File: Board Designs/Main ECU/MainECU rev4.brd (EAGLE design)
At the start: 120.6 x 78.9 mm, 164 parts, among them Q10 MMBT3904LT3G, Q11 MMBT3904LT3G, Q9 MMBT3904LT3G, X1 CONNECTOR-37, X2 CONNECTOR-4AUTOSPORT, X3 CONNECTOR-4NANO-FIT-VERTICAL-4, X4 CONNECTOR-4NANO-FIT-VERTICAL-4

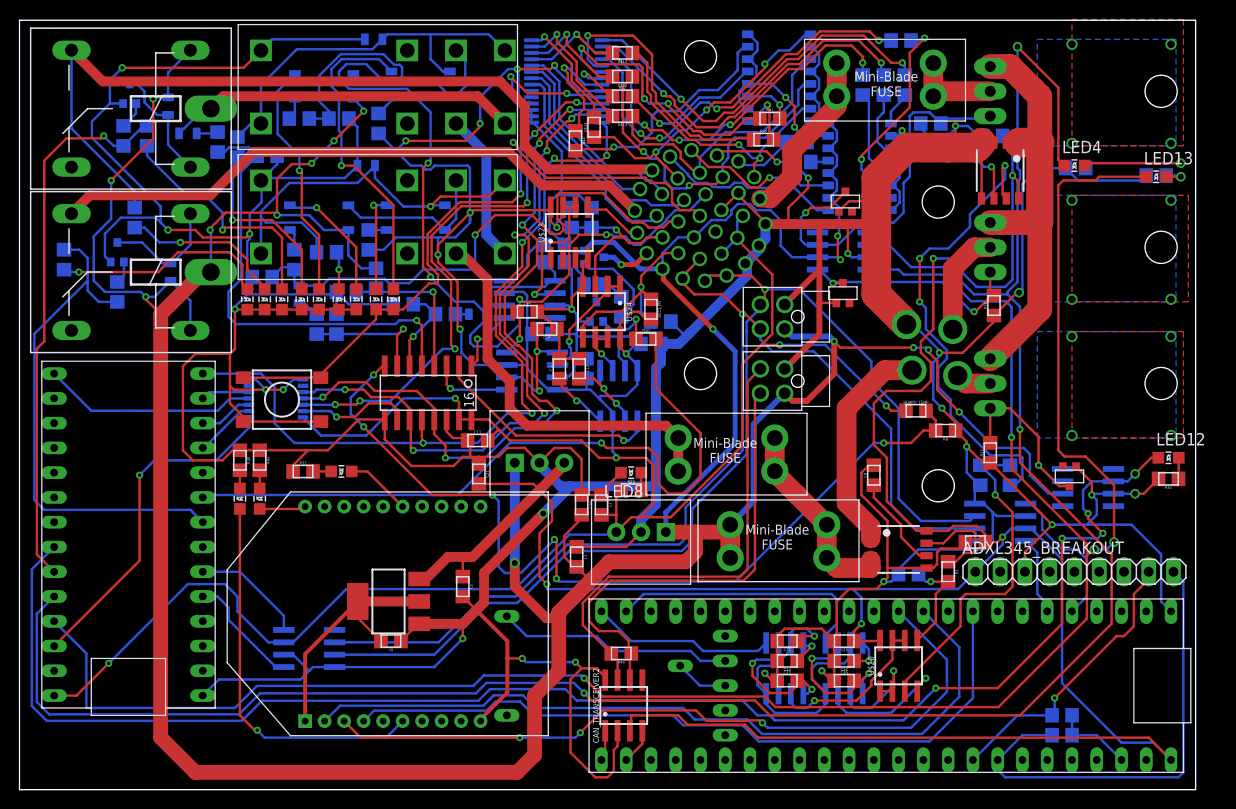
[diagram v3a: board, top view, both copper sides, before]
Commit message: Main ECU rev4: Flip transistors to top layer, widen inverter supply trace, move some resistors for easier soldering, adjust dashboard control resistor values, clean up schematic
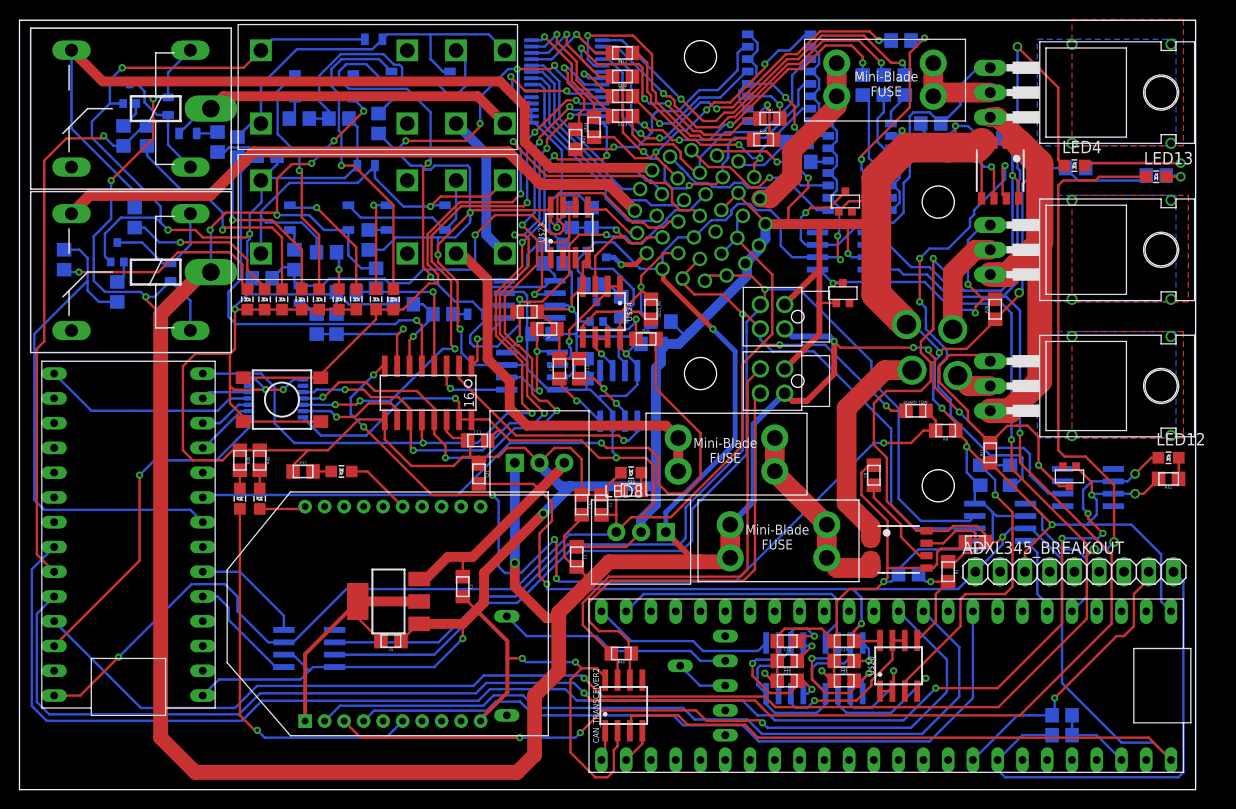
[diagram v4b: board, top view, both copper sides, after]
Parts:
- R35, R36, R38, R39, R40, R41, R42: value 2.2k -> 150
- R43: value 0 -> 150
- R44: value 2.2k -> 0
- moved R43 22.7 mm to (57.0, 66.7), flipped to the top, turned to 270 degrees
- moved R44 22.7 mm to (79.8, 66.4), flipped to the bottom, turned to 0 degrees
- moved R28 0.40 mm to (100.1, 49.3)
- moved R7 0.25 mm to (43.4, 48.8)
- moved U$15 0.25 mm to (59.2, 54.6)
- moved U$4 0.25 mm to (105.9, 55.4), flipped to the top, turned to 270 degrees
- moved U$6 0.25 mm to (105.9, 41.4), flipped to the top, turned to 270 degrees
- moved C10 0.25 mm to (99.8, 66.8)
- moved C19 0.18 mm to (54.7, 54.0)
- moved D2 0.13 mm to (46.9, 48.8)
- moved R18 0.13 mm to (24.9, 52.5)
- moved C17 0.13 mm to (54.7, 55.9)
- moved U$7 0.13 mm to (105.9, 71.5), flipped to the top, turned to 270 degrees
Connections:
- net DASH_CTRL8_OUT: now also R43.1; no longer R44.1
- net DASH_IO1: now also R44.2; no longer R43.2
- net N$57: now also R43.2; no longer R44.2
- net N$59: now also R44.1; no longer R43.1
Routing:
- net PUMPDRIVE: track 19.9 -> 32.3 mm
- net FAN2DRIVE: track 24.3 -> 31.8 mm, vias 2 -> 3
- net FAN2CONTROL: track 223.7 -> 220.1 mm
- net FAN1DRIVE: track 39.4 -> 42.7 mm
- net +12V: track 419.0 -> 417.5 mm
- net GND: track 845.5 -> 844.9 mm

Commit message: Main ECU rev{2,4}: Specify PNP transistor P/Ns
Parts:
- U$15: value BJT_PNPSOT -> SMMBT2907ALT1G
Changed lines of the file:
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@@
 </element>
 <element name="Q10" library="HyTechDevices" package="SOT23" value="MMBT3904LT3G" x="59.182" y="49.022" smashed="yes" rot="MR0"/>
-<element name="U$15" library="HyTechDevices" package="SOT23" value="BJT_PNPSOT" x="59.182" y="54.61" smashed="yes" rot="MR90"/>
+<element name="U$15" library="HyTechDevices" package="SOT23" value="SMMBT2907ALT1G" x="59.182" y="54.61" smashed="yes" rot="MR90"/>
 <element name="R10" library="HyTechDevices" package="0805" value="2.2k" x="64.262" y="46.228" smashed="yes">
 <attribute name="NAME" x="64.262" y="46.9519" size="0.3048" layer="25" align="bottom-center"/>

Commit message: Main ECU rev{1-4}: Add warning about RTC cell assembly, specify current sensor input capacitor value, lower XBee LED resistor to 33R; Main ECU rev{2,4}: Specify MCP3208 input capacitor value; Main ECU rev4: Lower relay-controlling transistors' base resistor to 1k; Main ECU rev5: make all relevant changes previously listed
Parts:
- C10, C9: value (none) -> 0.1uF
- C11: value (none) -> 1uF
- R45: value 2.3k -> 33
- R47, R50: value 2.2k -> 1k
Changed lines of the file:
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@@
 <attribute name="VALUE" x="56.4388" y="23.876" size="0.3048" layer="27" rot="R270" align="top-center"/>
 </element>
-<element name="C10" library="HyTechDevices" package="0805" value="" x="99.822" y="66.802" smashed="yes" rot="MR0">
+<element name="C10" library="HyTechDevices" package="0805" value="0.1uF" x="99.822" y="66.802" smashed="yes" rot="MR0">
 <attribute name="NAME" x="99.822" y="67.5259" size="0.3048" layer="26" rot="MR0" align="bottom-center" display="off"/>
 <attribute name="VALUE" x="99.822" y="66.0908" size="0.3048" layer="28" rot="MR0" align="top-center"/>
@@
 <attribute name="VALUE" x="88.3412" y="32.258" size="0.3048" layer="27" rot="R90" align="top-center"/>
 </element>
-<element name="C9" library="HyTechDevices" package="0805" value="" x="98.044" y="25.4" smashed="yes" rot="R180">
+<element name="C9" library="HyTechDevices" package="0805" value="0.1uF" x="98.044" y="25.4" smashed="yes" rot="R180">
 <attribute name="NAME" x="98.044" y="24.6761" size="0.3048" layer="25" rot="R180" align="bottom-center"/>
 <attribute name="VALUE" x="98.044" y="26.1112" size="0.3048" layer="27" rot="R180" align="top-center"/>
@@
 <attribute name="VALUE" x="79.756" y="65.7098" size="0.3048" layer="28" rot="MR0" align="top-center"/>
 </element>
-<element name="R45" library="HyTechDevices" package="0805" value="2.3k" x="24.638" y="33.782" smashed="yes" rot="R270">
+<element name="R45" library="HyTechDevices" package="0805" value="33" x="24.638" y="33.782" smashed="yes" rot="R270">
 <attribute name="NAME" x="25.3619" y="33.782" size="0.3048" layer="25" rot="R270" align="bottom-center"/>
 <attribute name="VALUE" x="23.9268" y="33.782" size="0.3048" layer="27" rot="R270" align="top-center"/>
@@
 <attribute name="VALUE" x="46.4058" y="32.385" size="0.3048" layer="27" rot="R270" align="top-center"/>
 </element>
-<element name="C11" library="HyTechDevices" package="0805" value="" x="46.99" y="35.814" smashed="yes">
+<element name="C11" library="HyTechDevices" package="0805" value="1uF" x="46.99" y="35.814" smashed="yes">
 <attribute name="NAME" x="46.99" y="36.5379" size="0.3048" layer="25" align="bottom-center"/>
 <attribute name="VALUE" x="46.99" y="35.1028" size="0.3048" layer="27" align="top-center"/>
@@
 </element>
 <element name="Q9" library="HyTechDevices" package="SOT23" value="MMBT3904LT3G" x="10.033" y="55.118" smashed="yes" rot="MR0"/>
-<element name="R47" library="HyTechDevices" package="0805" value="2.2k" x="10.033" y="51.054" smashed="yes" rot="MR90">
+<element name="R47" library="HyTechDevices" package="0805" value="1k" x="10.033" y="51.054" smashed="yes" rot="MR90">
 <attribute name="NAME" x="10.7569" y="51.054" size="0.3048" layer="26" rot="MR90" align="bottom-center"/>
 <attribute name="VALUE" x="9.3218" y="51.054" size="0.3048" layer="28" rot="MR90" align="top-center"/>
 </element>
 <element name="Q11" library="HyTechDevices" package="SOT23" value="MMBT3904LT3G" x="11.303" y="71.374" smashed="yes" rot="MR0"/>
-<element name="R50" library="HyTechDevices" package="0805" value="2.2k" x="10.668" y="67.056" smashed="yes" rot="MR90">
+<element name="R50" library="HyTechDevices" package="0805" value="1k" x="10.668" y="67.056" smashed="yes" rot="MR90">
 <attribute name="NAME" x="11.3919" y="67.056" size="0.3048" layer="26" rot="MR90" align="bottom-center"/>
 <attribute name="VALUE" x="9.9568" y="67.056" size="0.3048" layer="28" rot="MR90" align="top-center"/>

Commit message: Main ECU rev{1-5}: Update values of LED resistors based on testing
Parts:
- R11: value 43 -> 150
- R14, R21: value 820 -> 2k
- R16, R25, R32, R51, R52: value 100 -> 1.2k
- R17: value 820 -> 20k
- R31: value 1.2K -> 6.8k
- R45: value 33 -> 0
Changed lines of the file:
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@@
 <attribute name="VALUE" x="94.5388" y="22.352" size="0.3048" layer="27" rot="R270" align="top-center"/>
 </element>
-<element name="R11" library="HyTechDevices" package="0805" value="43" x="28.702" y="68.834" smashed="yes" rot="MR180">
+<element name="R11" library="HyTechDevices" package="0805" value="150" x="28.702" y="68.834" smashed="yes" rot="MR180">
 <attribute name="NAME" x="28.702" y="68.1101" size="0.3048" layer="26" rot="MR180" align="bottom-center"/>
 <attribute name="VALUE" x="28.702" y="69.5452" size="0.3048" layer="28" rot="MR180" align="top-center"/>
@@
 <attribute name="VALUE" x="36.1188" y="68.326" size="0.3048" layer="28" rot="MR90" align="top-center"/>
 </element>
-<element name="R14" library="HyTechDevices" package="0805" value="820" x="31.496" y="55.118" smashed="yes" rot="MR180">
+<element name="R14" library="HyTechDevices" package="0805" value="2k" x="31.496" y="55.118" smashed="yes" rot="MR180">
 <attribute name="NAME" x="31.496" y="54.3941" size="0.3048" layer="26" rot="MR180" align="bottom-center"/>
 <attribute name="VALUE" x="31.496" y="55.8292" size="0.3048" layer="28" rot="MR180" align="top-center"/>
@@
 <attribute name="VALUE" x="21.0312" y="66.421" size="0.3048" layer="28" rot="MR270" align="top-center"/>
 </element>
-<element name="R17" library="HyTechDevices" package="0805" value="820" x="22.352" y="65.913" smashed="yes" rot="MR270">
+<element name="R17" library="HyTechDevices" package="0805" value="20k" x="22.352" y="65.913" smashed="yes" rot="MR270">
 <attribute name="NAME" x="21.6281" y="65.913" size="0.3048" layer="26" rot="MR270" align="bottom-center"/>
 <attribute name="VALUE" x="23.0632" y="65.913" size="0.3048" layer="28" rot="MR270" align="top-center"/>
@@
 <attribute name="VALUE" x="62.738" y="30.0228" size="0.3048" layer="27" align="top-center"/>
 </element>
-<element name="R21" library="HyTechDevices" package="0805" value="820" x="28.194" y="54.356" smashed="yes" rot="MR90">
+<element name="R21" library="HyTechDevices" package="0805" value="2k" x="28.194" y="54.356" smashed="yes" rot="MR90">
 <attribute name="NAME" x="28.9179" y="54.356" size="0.3048" layer="26" rot="MR90" align="bottom-center"/>
 <attribute name="VALUE" x="27.4828" y="54.356" size="0.3048" layer="28" rot="MR90" align="top-center"/>
@@
 <attribute name="VALUE" x="21.8948" y="33.782" size="0.3048" layer="27" rot="R270" align="top-center"/>
 </element>
-<element name="R31" library="HyTechDevices" package="0805" value="1.2K" x="11.811" y="58.674" smashed="yes" rot="MR270">
+<element name="R31" library="HyTechDevices" package="0805" value="6.8k" x="11.811" y="58.674" smashed="yes" rot="MR270">
 <attribute name="NAME" x="11.0871" y="58.674" size="0.3048" layer="26" rot="MR270" align="bottom-center" display="off"/>
 <attribute name="VALUE" x="12.5222" y="58.674" size="0.3048" layer="28" rot="MR270" align="top-center" display="off"/>
 </element>
-<element name="R32" library="HyTechDevices" package="0805" value="100" x="29.083" y="32.639" smashed="yes">
+<element name="R32" library="HyTechDevices" package="0805" value="1.2k" x="29.083" y="32.639" smashed="yes">
 <attribute name="NAME" x="29.083" y="33.3629" size="0.3048" layer="25" align="bottom-center"/>
 <attribute name="VALUE" x="29.083" y="31.9278" size="0.3048" layer="27" align="top-center"/>
@@
 <attribute name="VALUE" x="79.756" y="65.7098" size="0.3048" layer="28" rot="MR0" align="top-center"/>
 </element>
-<element name="R45" library="HyTechDevices" package="0805" value="33" x="24.638" y="33.782" smashed="yes" rot="R270">
+<element name="R45" library="HyTechDevices" package="0805" value="0" x="24.638" y="33.782" smashed="yes" rot="R270">
 <attribute name="NAME" x="25.3619" y="33.782" size="0.3048" layer="25" rot="R270" align="bottom-center"/>
 <attribute name="VALUE" x="23.9268" y="33.782" size="0.3048" layer="27" rot="R270" align="top-center"/>
@@
 <element name="U$8" library="HyTechDevices" package="ZF112" value="G5LE" x="21.59" y="61.976" smashed="yes" rot="R180"/>
 <element name="LED6" library="HyTechDevices" package="LED-805" value="Red" x="23.368" y="50.292" smashed="yes" rot="R180"/>
-<element name="R16" library="HyTechDevices" package="0805" value="100" x="4.572" y="54.356" smashed="yes" rot="MR270">
+<element name="R16" library="HyTechDevices" package="0805" value="1.2k" x="4.572" y="54.356" smashed="yes" rot="MR270">
 <attribute name="NAME" x="3.8481" y="54.356" size="0.3048" layer="26" rot="MR270" align="bottom-center" display="off"/>
 <attribute name="VALUE" x="5.2832" y="54.356" size="0.3048" layer="28" rot="MR270" align="top-center" display="off"/>
@@
 <attribute name="VALUE" x="106.934" y="61.468" size="1.27" layer="27" ratio="10"/>
 </element>
-<element name="R25" library="HyTechDevices" package="0805" value="100" x="108.331" y="63.754" smashed="yes" rot="MR0">
+<element name="R25" library="HyTechDevices" package="0805" value="1.2k" x="108.331" y="63.754" smashed="yes" rot="MR0">
 <attribute name="NAME" x="108.331" y="64.4779" size="0.3048" layer="26" rot="MR0" align="bottom-center"/>
 <attribute name="VALUE" x="108.331" y="63.0428" size="0.3048" layer="28" rot="MR0" align="top-center"/>
@@
 <attribute name="VALUE" x="116.586" y="31.496" size="1.27" layer="27" ratio="10"/>
 </element>
-<element name="R51" library="HyTechDevices" package="0805" value="100" x="117.856" y="31.877" smashed="yes" rot="R180">
+<element name="R51" library="HyTechDevices" package="0805" value="1.2k" x="117.856" y="31.877" smashed="yes" rot="R180">
 <attribute name="NAME" x="117.856" y="31.1531" size="0.3048" layer="25" rot="R180" align="bottom-center"/>
 <attribute name="VALUE" x="117.856" y="32.5882" size="0.3048" layer="27" rot="R180" align="top-center"/>
@@
 <attribute name="VALUE" x="115.316" y="60.325" size="1.27" layer="27" ratio="10"/>
 </element>
-<element name="R52" library="HyTechDevices" package="0805" value="100" x="116.586" y="62.992" smashed="yes" rot="MR0">
+<element name="R52" library="HyTechDevices" package="0805" value="1.2k" x="116.586" y="62.992" smashed="yes" rot="MR0">
 <attribute name="NAME" x="116.586" y="63.7159" size="0.3048" layer="26" rot="MR0" align="bottom-center"/>
 <attribute name="VALUE" x="116.586" y="62.2808" size="0.3048" layer="28" rot="MR0" align="top-center"/>

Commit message: Main ECU rev{1-5}: Update values of OKI-78SR capacitors to 10uF
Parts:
- C1, C20: value .22uF -> 10uF
- C2, C21: value .1uF -> 10uF
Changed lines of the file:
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@@
 <attribute name="VALUE" x="91.948" y="38.1508" size="0.3048" layer="27" align="top-center"/>
 </element>
-<element name="C1" library="HyTechDevices" package="0805" value=".22uF" x="57.15" y="23.876" smashed="yes" rot="R270">
+<element name="C1" library="HyTechDevices" package="0805" value="10uF" x="57.15" y="23.876" smashed="yes" rot="R270">
 <attribute name="NAME" x="57.8739" y="23.876" size="0.3048" layer="25" rot="R270" align="bottom-center"/>
 <attribute name="VALUE" x="56.4388" y="23.876" size="0.3048" layer="27" rot="R270" align="top-center"/>
@@
 <attribute name="VALUE" x="99.822" y="66.0908" size="0.3048" layer="28" rot="MR0" align="top-center"/>
 </element>
-<element name="C2" library="HyTechDevices" package="0805" value=".1uF" x="59.69" y="29.21" smashed="yes" rot="R270">
+<element name="C2" library="HyTechDevices" package="0805" value="10uF" x="59.69" y="29.21" smashed="yes" rot="R270">
 <attribute name="NAME" x="60.4139" y="29.21" size="0.3048" layer="25" rot="R270" align="bottom-center"/>
 <attribute name="VALUE" x="58.9788" y="29.21" size="0.3048" layer="27" rot="R270" align="top-center"/>
@@
 <element name="U$16" library="HyTechDevices" package="CR-2450/G1AN" value="CR-2450/G1AN" x="62.6872" y="12.7" smashed="yes" rot="MR270"/>
 <element name="REG3" library="HyTechDevices" package="OKI-78SR" value="5V" x="53.34" y="33.528" smashed="yes"/>
-<element name="C20" library="HyTechDevices" package="0805" value=".22uF" x="57.658" y="29.21" smashed="yes" rot="R270">
+<element name="C20" library="HyTechDevices" package="0805" value="10uF" x="57.658" y="29.21" smashed="yes" rot="R270">
 <attribute name="NAME" x="58.3819" y="29.21" size="0.3048" layer="25" rot="R270" align="bottom-center"/>
 <attribute name="VALUE" x="56.9468" y="29.21" size="0.3048" layer="27" rot="R270" align="top-center"/>
 </element>
-<element name="C21" library="HyTechDevices" package="0805" value=".1uF" x="47.117" y="32.385" smashed="yes" rot="R270">
+<element name="C21" library="HyTechDevices" package="0805" value="10uF" x="47.117" y="32.385" smashed="yes" rot="R270">
 <attribute name="NAME" x="47.8409" y="32.385" size="0.3048" layer="25" rot="R270" align="bottom-center"/>
 <attribute name="VALUE" x="46.4058" y="32.385" size="0.3048" layer="27" rot="R270" align="top-center"/>
